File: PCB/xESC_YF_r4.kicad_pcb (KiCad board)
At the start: 2 copper layers, 49.5 x 29 mm, 39 parts, among them J1 Conn_01x09_Male, J10 OM-MB W => MC BRK, J11 Conn_01x04_Pin, J3 Conn_01x05_Male, J4 Conn_01x05_Male, J6 OM-MB U => MC SA, J7 Conn_01x06_Male, J8 Conn_01x06_Pin, J9 OM-MB V => MC +24V, Q1 BSS138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

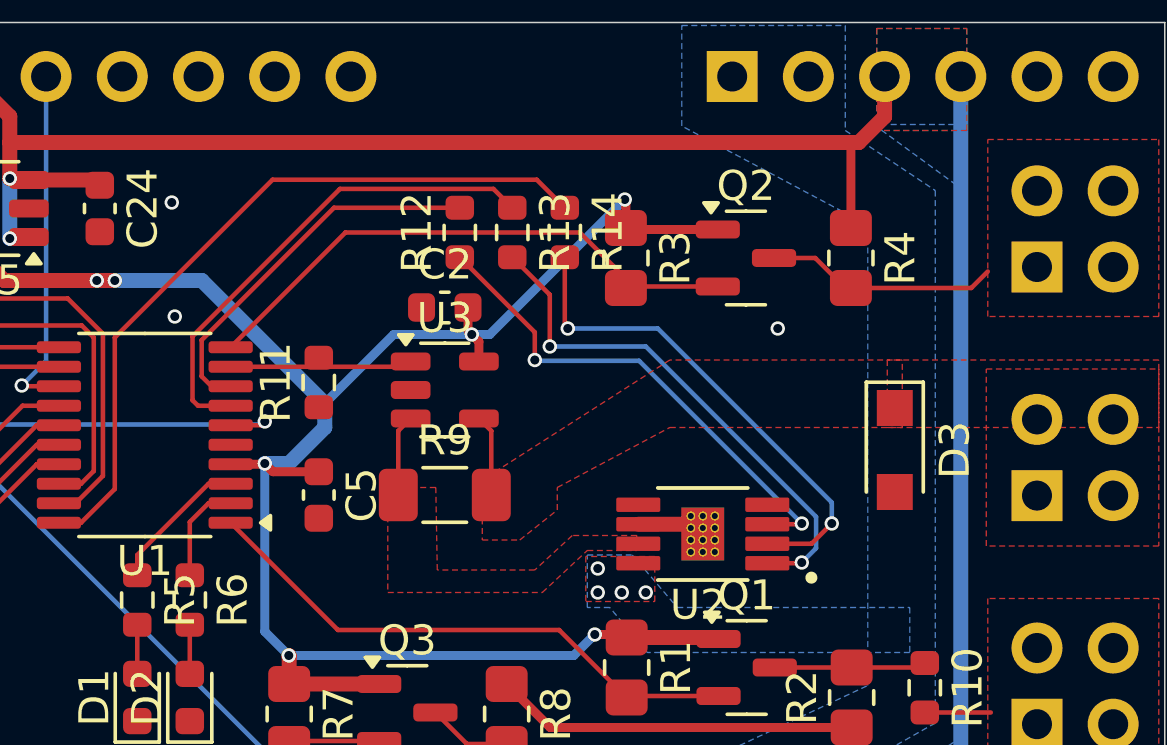
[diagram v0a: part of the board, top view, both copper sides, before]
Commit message: 2 stage current sense with 20/40 gain
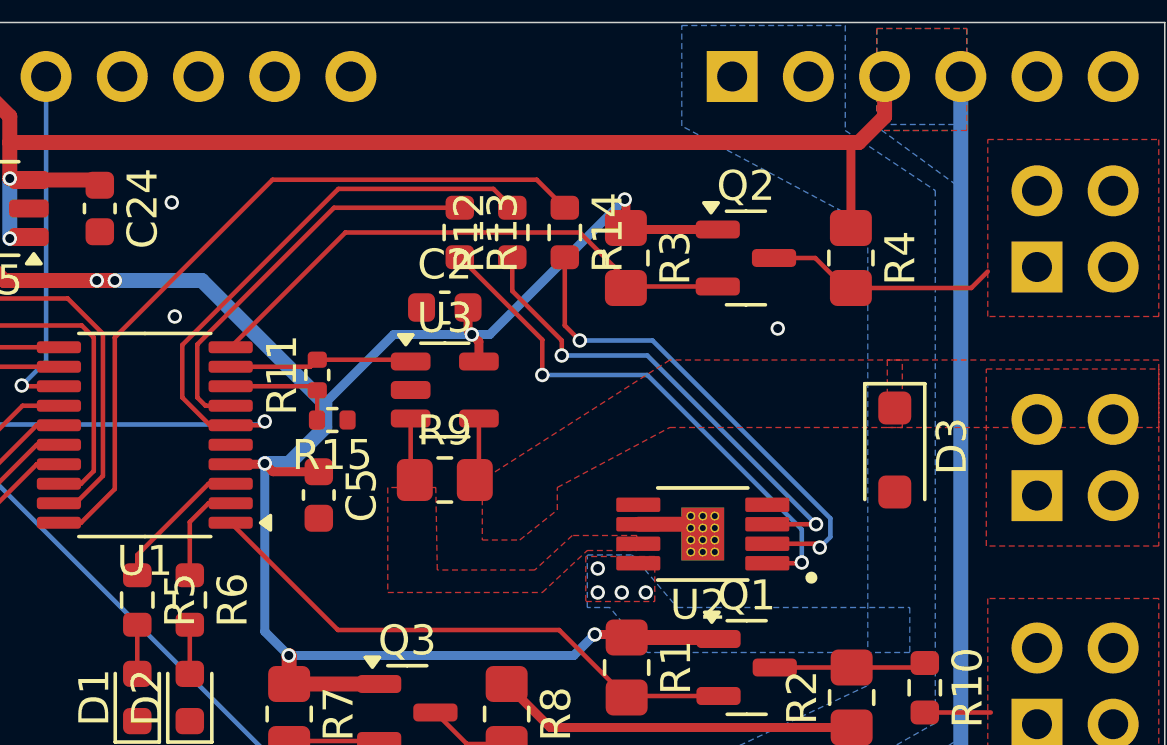
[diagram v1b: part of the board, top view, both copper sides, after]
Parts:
- added R15: 20k, Resistor_SMD:R_0402_1005Metric, F.Cu at (250.8, 117.2)
- D3: value PNE20020ER -> S2MW; footprint Diode_SMD:Nexperia_CFP3_SOD-123W -> Diode_SMD:D_SOD-123F
- R11: value 2k -> 20k; footprint Resistor_SMD:R_0603_1608Metric -> Resistor_SMD:R_0402_1005Metric
- R9: value 68mR -> 82mR; footprint Resistor_SMD:R_1206_3216Metric_Pad1.30x1.75mm_HandSolder -> Resistor_SMD:R_0805_2012Metric_Pad1.20x1.40mm_HandSolder
- moved R12 1.75 mm to (256.8, 110.9)
- moved R13 1.75 mm to (255.0, 110.9)
- moved R9 0.50 mm to (254.5, 119.2)
- moved R11 0.25 mm to (250.2, 115.7)
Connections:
- J3 pad 5: /NRST -> /~{VMS_FAULT}/NRST
- R11 pad 1: GND -> /CUR_SENSE_2
- R12 pad 2: /~{VMS_FAULT} -> /~{VMS_FAULT}/NRST
- U1 pad 6: /NRST -> /~{VMS_FAULT}/NRST
- U1 pad 8: /~{VMS_FAULT} -> /CUR_SENSE_2
- U2 pad 5: GND -> unconnected-(U2-DELAY-Pad5)
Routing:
- net /~{VMS_FAULT}/NRST: track 0.00 -> 36.3 mm, vias 0 -> 1
- net /NRST: track 19.1 -> 0.00 mm, vias 1 -> 0
- net /~{VMS_FAULT}: track 12.1 -> 0.00 mm
- net /CUR_SENSE_2: track 0.00 -> 3.73 mm
- net /VMS_IN: track 16.4 -> 13.6 mm
- net /VMS: track 2.72 -> 1.66 mm
- net /VMC: track 2.72 -> 1.66 mm
- net Net-(U2-IN): track 17.6 -> 18.1 mm

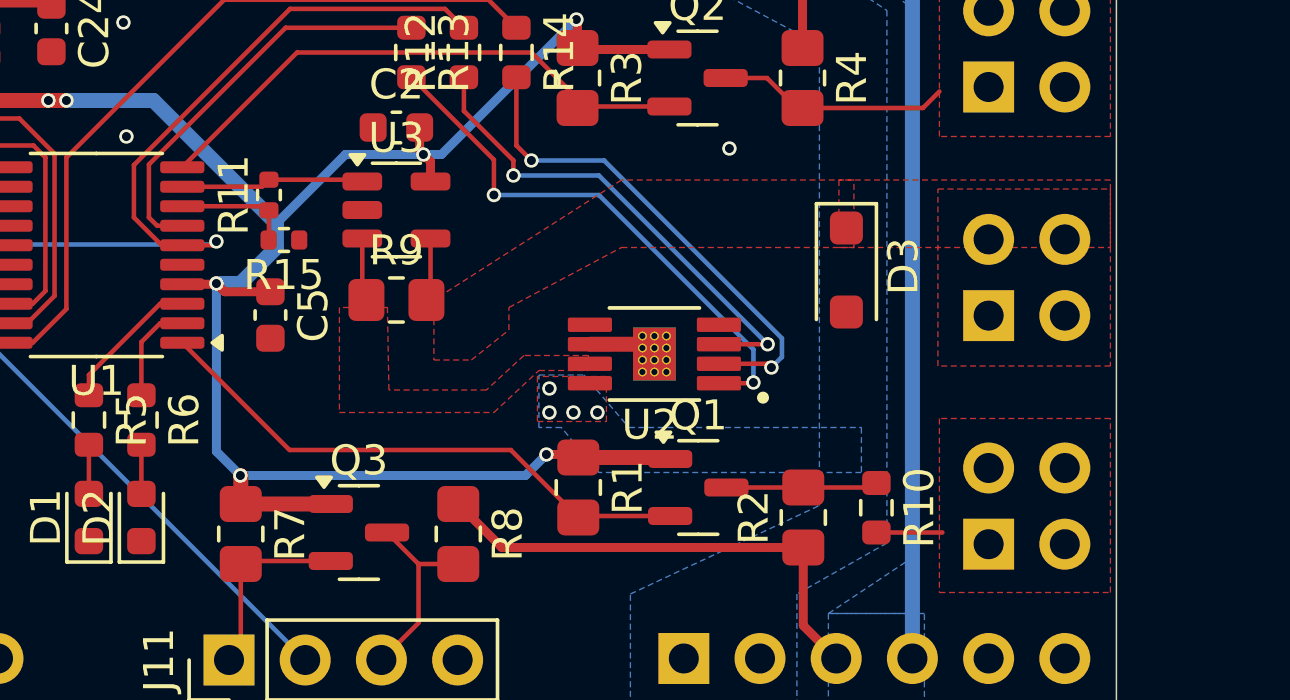
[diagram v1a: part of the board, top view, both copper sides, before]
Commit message: Open-load detection
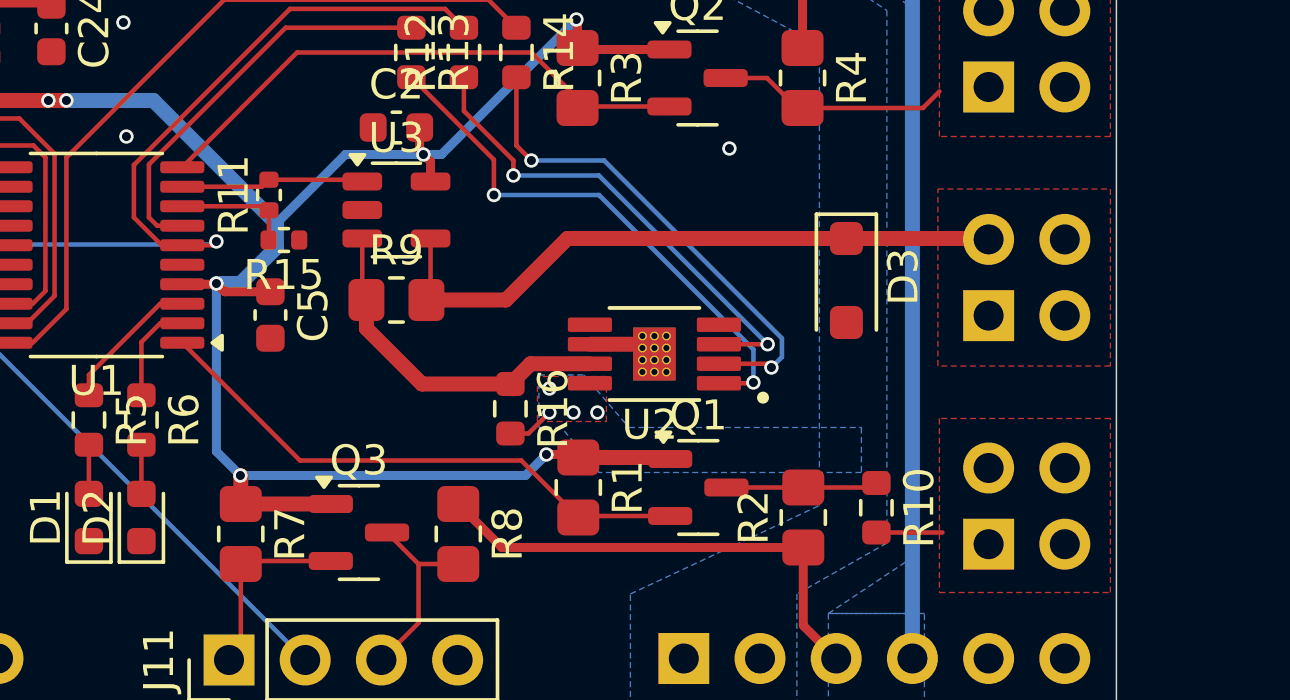
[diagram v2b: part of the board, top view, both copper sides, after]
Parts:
- added R16: 15k, Resistor_SMD:R_0603_1608Metric, F.Cu at (258.3, 122.8)
- moved D3 0.35 mm to (269.5, 118.5)
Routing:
- net /VMC: track 1.66 -> 21.3 mm
- net /VMS: track 1.66 -> 11.1 mm
- net VM: track 0.00 -> 1.59 mm
- removed copper zone on F.Cu, net /VMS

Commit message: Fix DRC issues
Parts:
- U2: footprint TPS1H200AQDGNRQ1:SOP65P490X110-9N-AHMOD -> TPS1H200AQDGNRQ1.snapeda:SOP65P490X110-9N
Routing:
- net GND: track 1.82 -> 2.65 mm, vias 5 -> 7
- net +5V: track 84.1 -> 84.8 mm, vias 2 -> 3
- net +3V3: track 73.5 -> 73.4 mm, vias 7 -> 6
